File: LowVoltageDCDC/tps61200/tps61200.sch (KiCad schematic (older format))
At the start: 10 parts

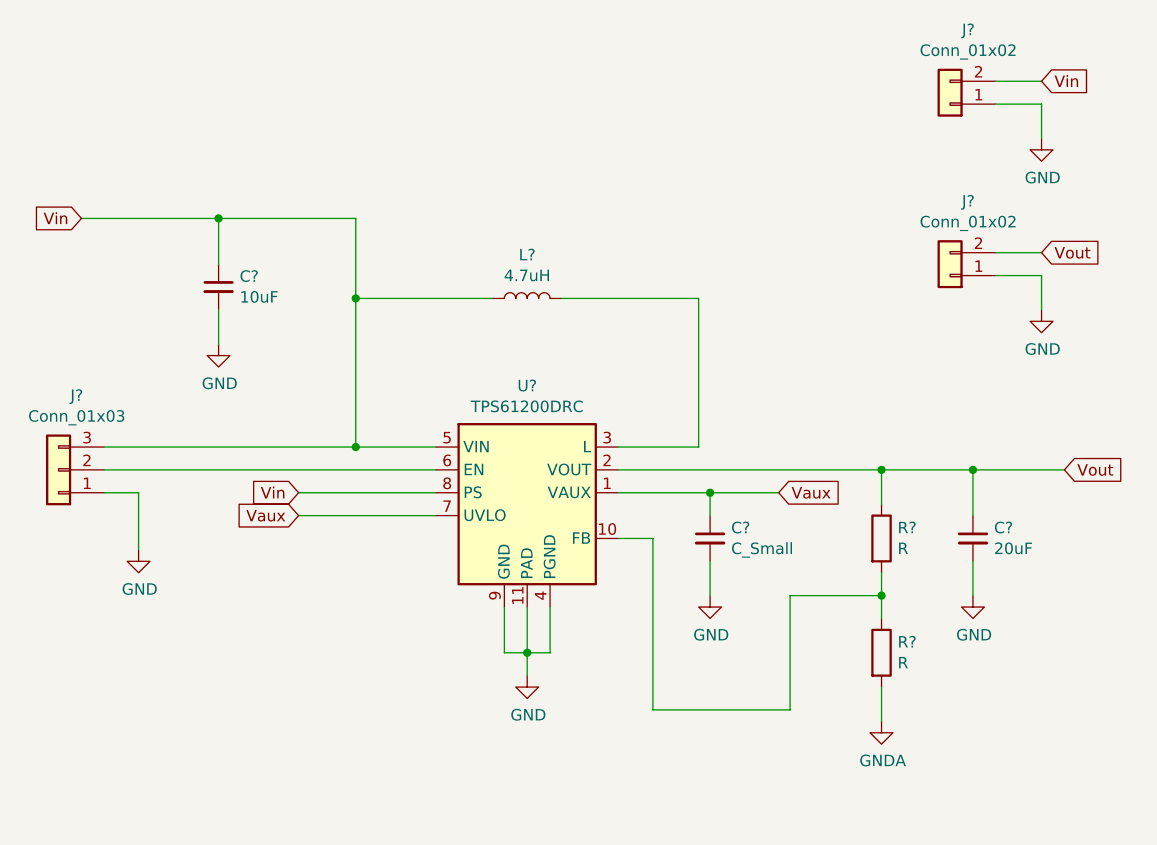
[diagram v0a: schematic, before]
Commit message: finalizado esquematico, falta associar os componentes
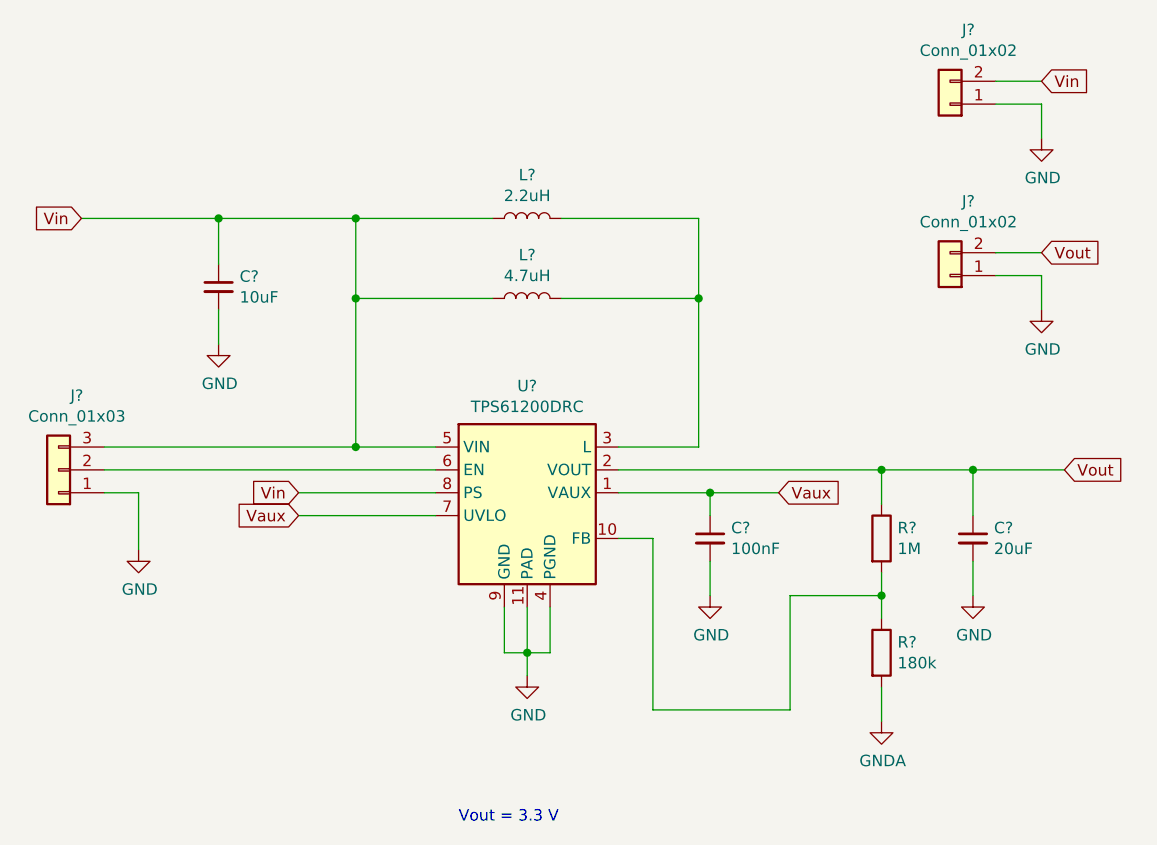
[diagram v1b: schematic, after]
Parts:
- added L?: 2.2uH, symbol Device:L
- C?: value C_Small -> 100nF
- R?: value R -> 180k
- R?: value R -> 1M
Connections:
- net Vin: now also L?.1
- net at L?.2, U?.3 (L): now also L?.2
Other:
- note added: "Vout = 3.3 V\n"
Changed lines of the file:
@@
 Wire Wire Line
 	4050 3250 3900 3250
-Text GLabel 4750 3350 0    50   Input ~ 0
-Vaux
-Wire Wire Line
-	4750 3350 5350 3350
 Text GLabel 3800 2050 0    50   Input ~ 0
 Vin
@@
 P 7300 3950
 F 0 "R?" H 7370 3996 50  0000 L CNN
-F 1 "R" H 7370 3905 50  0000 L CNN
+F 1 "180k" H 7370 3905 50  0000 L CNN
 F 2 "" V 7230 3950 50  0001 C CNN
 F 3 "~" H 7300 3950 50  0001 C CNN
@@
 P 7300 3450
 F 0 "R?" H 7370 3496 50  0000 L CNN
-F 1 "R" H 7370 3405 50  0000 L CNN
+F 1 "1M" H 7370 3405 50  0000 L CNN
 F 2 "" V 7230 3450 50  0001 C CNN
 F 3 "~" H 7300 3450 50  0001 C CNN
@@
 P 6550 3450
 F 0 "C?" H 6642 3496 50  0000 L CNN
-F 1 "C_Small" H 6642 3405 50  0000 L CNN
+F 1 "100nF" H 6642 3405 50  0000 L CNN
 F 2 "" H 6550 3450 50  0001 C CNN
 F 3 "~" H 6550 3450 50  0001 C CNN
@@
 Wire Wire Line
 	8000 2300 7800 2300
+$Comp
+L Device:L L?
+U 1 1 5C54CDCA
+P 5750 2050
+F 0 "L?" V 5940 2050 50  0000 C CNN
+F 1 "2.2uH" V 5849 2050 50  0000 C CNN
+F 2 "" H 5750 2050 50  0001 C CNN
+F 3 "~" H 5750 2050 50  0001 C CNN
+	1    5750 2050
+	0    -1   -1   0
+$EndComp
+Wire Wire Line
+	5600 2050 5000 2050
+Connection ~ 5000 2050
+Wire Wire Line
+	5900 2050 6500 2050
+Wire Wire Line
+	6500 2050 6500 2400
+Connection ~ 6500 2400
+Wire Wire Line
+	4750 3350 5350 3350
+Text GLabel 4750 3350 0    50   Input ~ 0
+Vaux
+Text Notes 5450 4700 0    50   ~ 0
+Vout = 3.3 V\n
 $EndSCHEMATC

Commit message: algumas melhorias
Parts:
- removed L?: 2.2uH, symbol Device:L
- added C4: 100nF, Capacitor_SMD:C_0805_2012Metric_Pad1.15x1.40mm_HandSolder, symbol Device:C_Small
- C1: renamed from C?; footprint (none) -> Capacitor_SMD:C_0805_2012Metric_Pad1.15x1.40mm_HandSolder
- C2: renamed from C?; value 100nF -> 1uF; footprint (none) -> Capacitor_SMD:C_0805_2012Metric_Pad1.15x1.40mm_HandSolder
- C3: renamed from C?; footprint (none) -> Capacitor_SMD:C_1206_3216Metric_Pad1.42x1.75mm_HandSolder
- J1: renamed from J?; footprint (none) -> Connector_PinSocket_2.54mm:PinSocket_1x03_P2.54mm_Vertical
- J2, J3: renamed from J?; footprint (none) -> Connector_PinSocket_2.54mm:PinSocket_1x02_P2.54mm_Vertical
- L1: renamed from L?; value 4.7uH -> 3.3 uH; footprint (none) -> Inductor_SMD:L_Taiyo-Yuden_NR-60xx_HandSoldering
- R1, R2: renamed from R?; footprint (none) -> Resistor_SMD:R_0805_2012Metric_Pad1.15x1.40mm_HandSolder
- gave numbers to parts that had none: 1
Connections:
- net GND: now also C4.2
- net Vin: now also C4.1
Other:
- moved on the sheet: C1
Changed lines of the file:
@@
 $EndDescr
 $Comp
-L Regulator_Switching:TPS61200DRC U?
+L Regulator_Switching:TPS61200DRC U1
 U 1 1 5C5333CD
 P 5750 3250
-F 0 "U?" H 5750 3717 50  0000 C CNN
+F 0 "U1" H 5750 3717 50  0000 C CNN
 F 1 "TPS61200DRC" H 5750 3626 50  0000 C CNN
 F 2 "Package_SON:Texas_S-PVSON-N10_ThermalVias" H 5750 2800 50  0001 C CNN
@@
 $EndComp
 $Comp
-L power:GND #PWR?
+L power:GND #PWR0101
 U 1 1 5C533440
 P 5750 4050
-F 0 "#PWR?" H 5750 3800 50  0001 C CNN
+F 0 "#PWR0101" H 5750 3800 50  0001 C CNN
 F 1 "GND" H 5755 3877 50  0000 C CNN
 F 2 "" H 5750 4050 50  0001 C CNN
@@
 	5850 3950 5750 3950
 $Comp
-L Connector_Generic:Conn_01x03 J?
+L Connector_Generic:Conn_01x03 J1
 U 1 1 5C533751
 P 3700 3150
-F 0 "J?" H 3620 2825 50  0000 C CNN
+F 0 "J1" H 3620 2825 50  0000 C CNN
 F 1 "Conn_01x03" H 3620 2916 50  0000 C CNN
-F 2 "" H 3700 3150 50  0001 C CNN
+F 2 "Connector_PinSocket_2.54mm:PinSocket_1x03_P2.54mm_Vertical" H 3700 3150 50  0001 C CNN
 F 3 "~" H 3700 3150 50  0001 C CNN
 	1    3700 3150
@@
 	5350 3150 3900 3150
 $Comp
-L power:GND #PWR?
+L power:GND #PWR0102
 U 1 1 5C5337BF
 P 4050 3500
-F 0 "#PWR?" H 4050 3250 50  0001 C CNN
+F 0 "#PWR0102" H 4050 3250 50  0001 C CNN
 F 1 "GND" H 4055 3327 50  0000 C CNN
 F 2 "" H 4050 3500 50  0001 C CNN
@@
 Vin
 Wire Wire Line
-	3800 2050 4400 2050
+	3800 2050 4150 2050
 Wire Wire Line
 	5000 2050 5000 2400
@@
 Connection ~ 5000 3050
 $Comp
-L Device:C_Small C?
+L Device:C_Small C1
 U 1 1 5C533AC2
-P 4400 2350
-F 0 "C?" H 4492 2396 50  0000 L CNN
-F 1 "10uF" H 4492 2305 50  0000 L CNN
-F 2 "" H 4400 2350 50  0001 C CNN
-F 3 "~" H 4400 2350 50  0001 C CNN
-	1    4400 2350
-	1    0    0    -1
-$EndComp
-$Comp
-L power:GND #PWR?
+P 4150 2350
+F 0 "C1" H 4242 2396 50  0000 L CNN
+F 1 "10uF" H 4242 2305 50  0000 L CNN
+F 2 "Capacitor_SMD:C_0805_2012Metric_Pad1.15x1.40mm_HandSolder" H 4150 2350 50  0001 C CNN
+F 3 "~" H 4150 2350 50  0001 C CNN
+	1    4150 2350
+	1    0    0    -1
+$EndComp
+$Comp
+L power:GND #PWR0103
 U 1 1 5C533AF8
-P 4400 2600
-F 0 "#PWR?" H 4400 2350 50  0001 C CNN
-F 1 "GND" H 4405 2427 50  0000 C CNN
-F 2 "" H 4400 2600 50  0001 C CNN
-F 3 "" H 4400 2600 50  0001 C CNN
-	1    4400 2600
-	1    0    0    -1
-$EndComp
-Wire Wire Line
-	4400 2250 4400 2050
-Connection ~ 4400 2050
-Wire Wire Line
-	4400 2050 5000 2050
-Wire Wire Line
-	4400 2450 4400 2600
+P 4150 2600
+F 0 "#PWR0103" H 4150 2350 50  0001 C CNN
+F 1 "GND" H 4155 2427 50  0000 C CNN
+F 2 "" H 4150 2600 50  0001 C CNN
+F 3 "" H 4150 2600 50  0001 C CNN
+	1    4150 2600
+	1    0    0    -1
+$EndComp
+Wire Wire Line
+	4150 2250 4150 2050
+Wire Wire Line
+	4150 2450 4150 2600
 Text GLabel 4750 3250 0    50   Input ~ 0
 Vin
@@
 	4750 3250 5350 3250
 $Comp
-L Device:L L?
+L Device:L L1
 U 1 1 5C533F3C
 P 5750 2400
-F 0 "L?" V 5940 2400 50  0000 C CNN
-F 1 "4.7uH" V 5849 2400 50  0000 C CNN
-F 2 "" H 5750 2400 50  0001 C CNN
+F 0 "L1" V 5940 2400 50  0000 C CNN
+F 1 "3.3 uH" V 5849 2400 50  0000 C CNN
+F 2 "Inductor_SMD:L_Taiyo-Yuden_NR-60xx_HandSoldering" H 5750 2400 50  0001 C CNN
 F 3 "~" H 5750 2400 50  0001 C CNN
 	1    5750 2400
@@
 	6500 3050 6150 3050
 $Comp
-L Device:R R?
+L Device:R R2
 U 1 1 5C53439C
 P 7300 3950
-F 0 "R?" H 7370 3996 50  0000 L CNN
+F 0 "R2" H 7370 3996 50  0000 L CNN
 F 1 "180k" H 7370 3905 50  0000 L CNN
-F 2 "" V 7230 3950 50  0001 C CNN
+F 2 "Resistor_SMD:R_0805_2012Metric_Pad1.15x1.40mm_HandSolder" V 7230 3950 50  0001 C CNN
 F 3 "~" H 7300 3950 50  0001 C CNN
 	1    7300 3950
@@
 $EndComp
 $Comp
-L Device:R R?
+L Device:R R1
 U 1 1 5C534424
 P 7300 3450
-F 0 "R?" H 7370 3496 50  0000 L CNN
+F 0 "R1" H 7370 3496 50  0000 L CNN
 F 1 "1M" H 7370 3405 50  0000 L CNN
-F 2 "" V 7230 3450 50  0001 C CNN
+F 2 "Resistor_SMD:R_0805_2012Metric_Pad1.15x1.40mm_HandSolder" V 7230 3450 50  0001 C CNN
 F 3 "~" H 7300 3450 50  0001 C CNN
 	1    7300 3450
@@
 	7300 3150 6150 3150
 $Comp
-L power:GNDA #PWR?
+L power:GNDA #PWR0104
 U 1 1 5C534BC8
 P 7300 4250
-F 0 "#PWR?" H 7300 4000 50  0001 C CNN
+F 0 "#PWR0104" H 7300 4000 50  0001 C CNN
 F 1 "GNDA" H 7305 4077 50  0000 C CNN
 F 2 "" H 7300 4250 50  0001 C CNN
@@
 	7300 4250 7300 4100
 $Comp
-L Device:C_Small C?
+L Device:C_Small C2
 U 1 1 5C534EDB
 P 6550 3450
-F 0 "C?" H 6642 3496 50  0000 L CNN
-F 1 "100nF" H 6642 3405 50  0000 L CNN
-F 2 "" H 6550 3450 50  0001 C CNN
+F 0 "C2" H 6642 3496 50  0000 L CNN
+F 1 "1uF" H 6642 3405 50  0000 L CNN
+F 2 "Capacitor_SMD:C_0805_2012Metric_Pad1.15x1.40mm_HandSolder" H 6550 3450 50  0001 C CNN
 F 3 "~" H 6550 3450 50  0001 C CNN
 	1    6550 3450
@@
 	6550 3250 6150 3250
 $Comp
-L power:GND #PWR?
+L power:GND #PWR0105
 U 1 1 5C535216
 P 6550 3700
-F 0 "#PWR?" H 6550 3450 50  0001 C CNN
+F 0 "#PWR0105" H 6550 3450 50  0001 C CNN
 F 1 "GND" H 6555 3527 50  0000 C CNN
 F 2 "" H 6550 3700 50  0001 C CNN
@@
 Connection ~ 6550 3250
 $Comp
-L Device:C_Small C?
+L Device:C_Small C3
 U 1 1 5C535E18
 P 7700 3450
-F 0 "C?" H 7792 3496 50  0000 L CNN
+F 0 "C3" H 7792 3496 50  0000 L CNN
 F 1 "20uF" H 7792 3405 50  0000 L CNN
-F 2 "" H 7700 3450 50  0001 C CNN
+F 2 "Capacitor_SMD:C_1206_3216Metric_Pad1.42x1.75mm_HandSolder" H 7700 3450 50  0001 C CNN
 F 3 "~" H 7700 3450 50  0001 C CNN
 	1    7700 3450
@@
 	7700 3350 7700 3150
 $Comp
-L power:GND #PWR?
+L power:GND #PWR0106
 U 1 1 5C536384
 P 7700 3700
-F 0 "#PWR?" H 7700 3450 50  0001 C CNN
+F 0 "#PWR0106" H 7700 3450 50  0001 C CNN
 F 1 "GND" H 7705 3527 50  0000 C CNN
 F 2 "" H 7700 3700 50  0001 C CNN
@@
 	7300 3700 7300 3800
 $Comp
-L Connector_Generic:Conn_01x02 J?
+L Connector_Generic:Conn_01x02 J2
 U 1 1 5C538C56
 P 7600 1550
-F 0 "J?" H 7520 1225 50  0000 C CNN
+F 0 "J2" H 7520 1225 50  0000 C CNN
 F 1 "Conn_01x02" H 7520 1316 50  0000 C CNN
-F 2 "" H 7600 1550 50  0001 C CNN
+F 2 "Connector_PinSocket_2.54mm:PinSocket_1x02_P2.54mm_Vertical" H 7600 1550 50  0001 C CNN
 F 3 "~" H 7600 1550 50  0001 C CNN
 	1    7600 1550
@@
 Vin
 $Comp
-L power:GND #PWR?
+L power:GND #PWR0107
 U 1 1 5C538D52
 P 8000 1700
-F 0 "#PWR?" H 8000 1450 50  0001 C CNN
+F 0 "#PWR0107" H 8000 1450 50  0001 C CNN
 F 1 "GND" H 8005 1527 50  0000 C CNN
 F 2 "" H 8000 1700 50  0001 C CNN
@@
 	7800 1450 8000 1450
 $Comp
-L Connector_Generic:Conn_01x02 J?
+L Connector_Generic:Conn_01x02 J3
 U 1 1 5C539A10
 P 7600 2300
-F 0 "J?" H 7520 1975 50  0000 C CNN
+F 0 "J3" H 7520 1975 50  0000 C CNN
 F 1 "Conn_01x02" H 7520 2066 50  0000 C CNN
-F 2 "" H 7600 2300 50  0001 C CNN
+F 2 "Connector_PinSocket_2.54mm:PinSocket_1x02_P2.54mm_Vertical" H 7600 2300 50  0001 C CNN
 F 3 "~" H 7600 2300 50  0001 C CNN
 	1    7600 2300
@@
 	8000 2200 7800 2200
 $Comp
-L power:GND #PWR?
+L power:GND #PWR0108
 U 1 1 5C53A8AD
 P 8000 2450
-F 0 "#PWR?" H 8000 2200 50  0001 C CNN
+F 0 "#PWR0108" H 8000 2200 50  0001 C CNN
 F 1 "GND" H 8005 2277 50  0000 C CNN
 F 2 "" H 8000 2450 50  0001 C CNN
@@
 Wire Wire Line
 	8000 2300 7800 2300
-$Comp
-L Device:L L?
-U 1 1 5C54CDCA
-P 5750 2050
-F 0 "L?" V 5940 2050 50  0000 C CNN
-F 1 "2.2uH" V 5849 2050 50  0000 C CNN
-F 2 "" H 5750 2050 50  0001 C CNN
-F 3 "~" H 5750 2050 50  0001 C CNN
-	1    5750 2050
-	0    -1   -1   0
-$EndComp
-Wire Wire Line
-	5600 2050 5000 2050
-Connection ~ 5000 2050
-Wire Wire Line
-	5900 2050 6500 2050
-Wire Wire Line
-	6500 2050 6500 2400
-Connection ~ 6500 2400
 Wire Wire Line
 	4750 3350 5350 3350
@@
 Text Notes 5450 4700 0    50   ~ 0
 Vout = 3.3 V\n
+Connection ~ 4150 2050
+Wire Wire Line
+	4150 2050 4550 2050
+$Comp
+L Device:C_Small C4
+U 1 1 5C582025
+P 4550 2350
+F 0 "C4" H 4642 2396 50  0000 L CNN
+F 1 "100nF" H 4642 2305 50  0000 L CNN
+F 2 "Capacitor_SMD:C_0805_2012Metric_Pad1.15x1.40mm_HandSolder" H 4550 2350 50  0001 C CNN
+F 3 "~" H 4550 2350 50  0001 C CNN
+	1    4550 2350
+	1    0    0    -1
+$EndComp
+Wire Wire Line
+	4550 2050 4550 2250
+Connection ~ 4550 2050
+Wire Wire Line
+	4550 2050 5000 2050
+$Comp
+L power:GND #PWR0109
+U 1 1 5C5828D2
+P 4550 2600
+F 0 "#PWR0109" H 4550 2350 50  0001 C CNN
+F 1 "GND" H 4555 2427 50  0000 C CNN
+F 2 "" H 4550 2600 50  0001 C CNN
+F 3 "" H 4550 2600 50  0001 C CNN
+	1    4550 2600
+	1    0    0    -1
+$EndComp
+Wire Wire Line
+	4550 2600 4550 2450
 $EndSCHEMATC
